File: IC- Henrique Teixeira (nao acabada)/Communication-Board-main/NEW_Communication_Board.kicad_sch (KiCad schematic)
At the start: 69 parts, among them J1 USB_IN, J2 IMU, J3 Mini Fuse Socket, J4 XM_conn, J5 HUB-3, J6 HUB-4, U1 FE1.1s, U2 FT232RL, U3 FT232RL, U4 MAX485E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

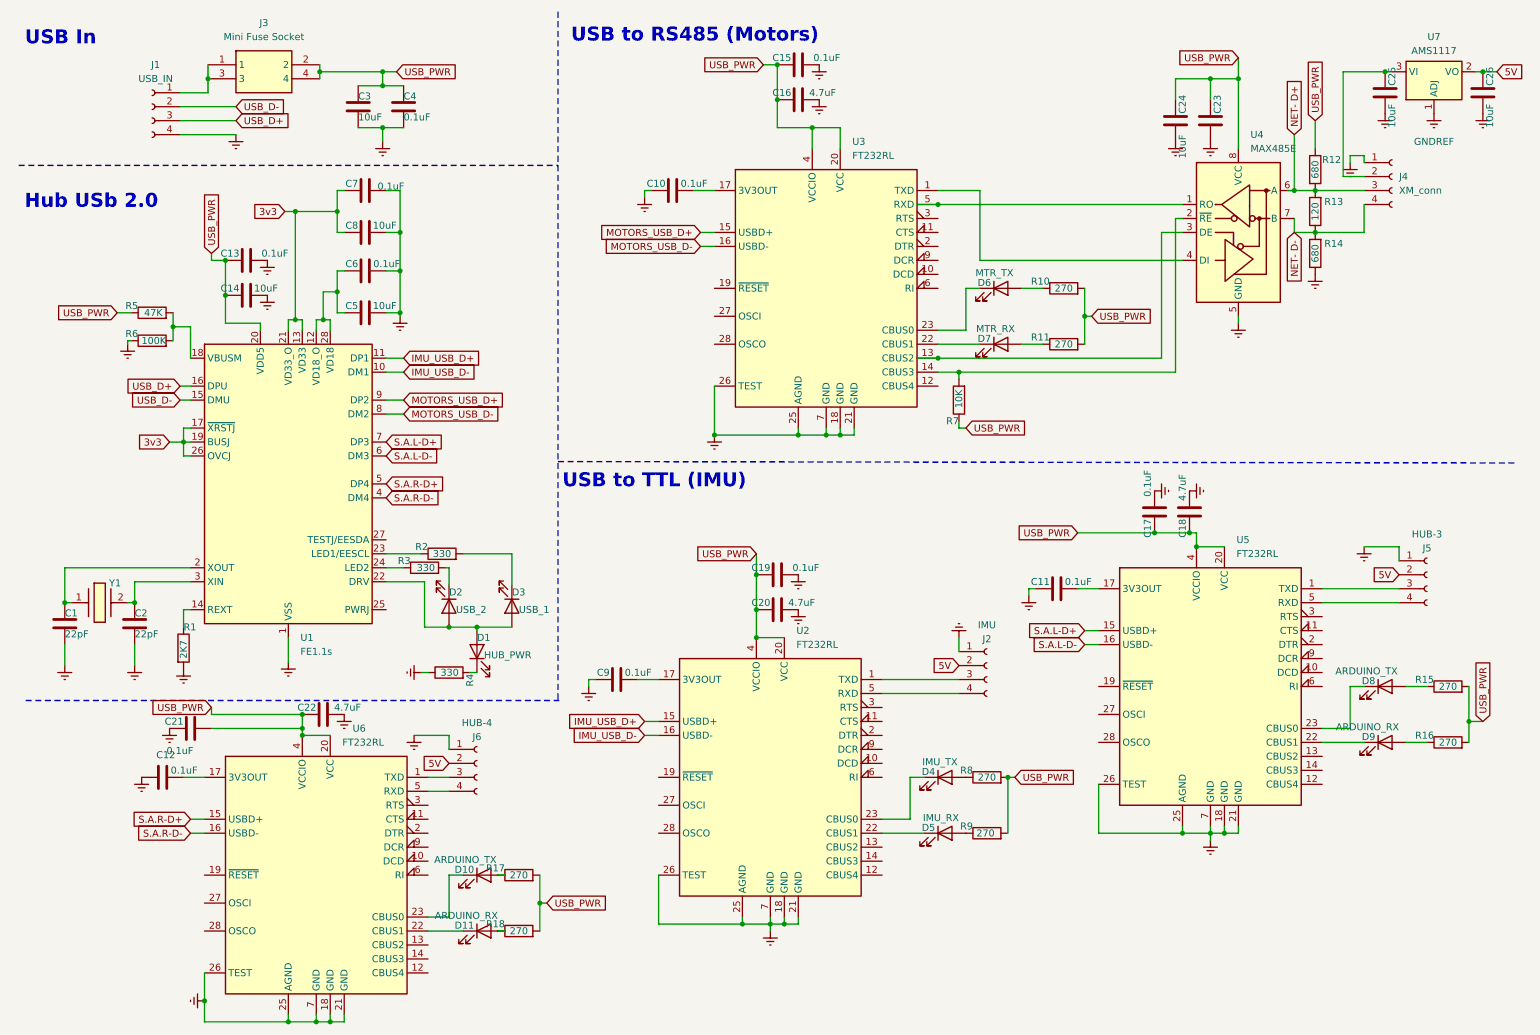
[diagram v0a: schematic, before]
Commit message: V2 communication Board
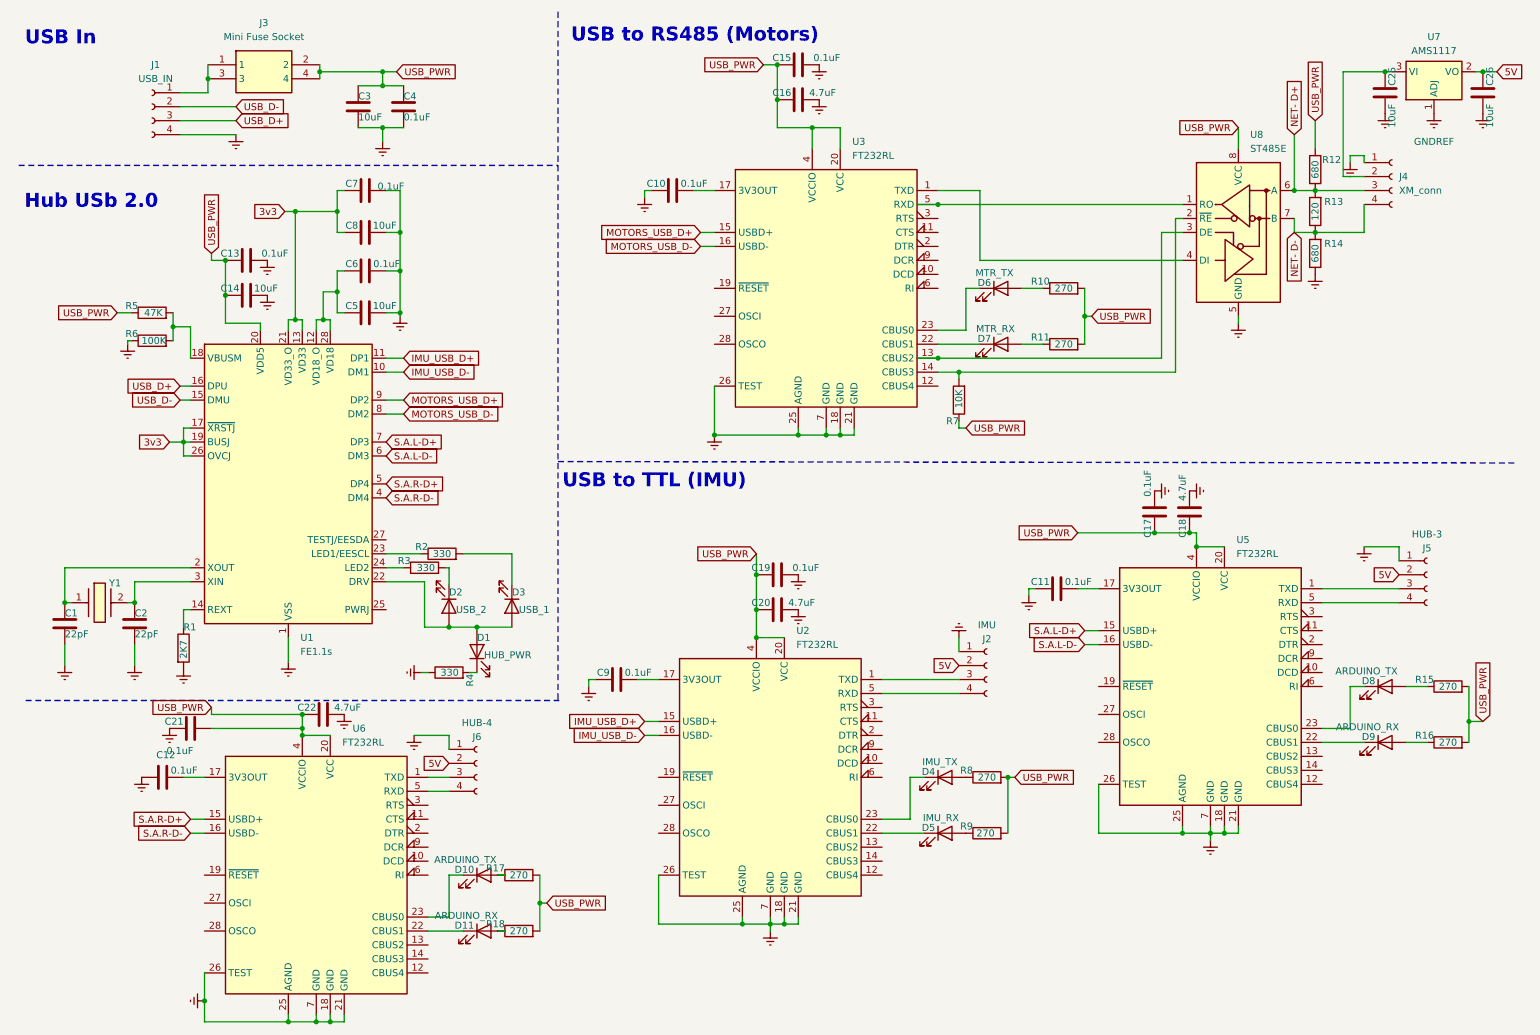
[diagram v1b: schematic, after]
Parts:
- removed C23: 0.1uF, Capacitor_SMD:C_1206_3216Metric, symbol Device:C
- removed C24: 10uF, Capacitor_SMD:C_1206_3216Metric, symbol Device:C
- removed U4: MAX485E, Package_SO:SOIC-8_3.9x4.9mm_P1.27mm, symbol Interface_UART:MAX485E
- added U8: ST485E, Package_SO:SOIC-8_3.9x4.9mm_P1.27mm, symbol Interface_UART:ST485E
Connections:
- net GNDREF: now also U8.5 (GND)
- net NET- D+: now also U8.6 (A)
- net NET- D-: now also U8.7 (B)
- net USB_PWR: now also U8.8 (VCC)
- net at U3.1 (TXD): now also U8.4 (DI)
- net at U3.13 (CBUS2): now also U8.3 (DE)
- net at R7.2, U3.14 (CBUS3): now also U8.2 (~{RE})
- net at U3.5 (RXD): now also U8.1 (RO)
